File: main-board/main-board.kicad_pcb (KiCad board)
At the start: 2 copper layers, 56 parts, among them J1 MOTOR0, J10 PROGRAMMER, J11 CAM0, J12 CAM1, J13 CAM2, J14 CAM3, J15 CAM4, J16 CAM5, J17 CAM6, J18 CAM7, J19 PowerBoard Interface, J2 MOTOR1, J20 IMU Breakout, J3 MOTOR2, J4 MOTOR3, J5 RJ45, J6 MOTOR4, J7 MOTOR5, J8 MOTOR6, J9 MOTOR7, SW1 SW_SPST, T1 ATB2012E-50011M-T01, T2 ATB2012E-50011M-T01, U1 MCP2515-EST, U2 ATA6560, U3 ATmega2560-16AU | Main Proc, U4 MC14051B, U5 MC14051B, U6 SN75HVD3082EDR, U7 LTC1983ES6-5-TRPBF, U8 OPAMP, U9 OPAMP, Y1 20MHz, Y2 20MHz

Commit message: populate components
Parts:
- moved C6 147.5 mm to (89.9, 121.2), turned to 180 degrees
- moved R11 126.9 mm to (86.6, 85.3), turned to 270 degrees
- moved C2 122.9 mm to (93.8, 93.0), turned to 90 degrees
- moved C1 122.7 mm to (93.8, 89.6), turned to 270 degrees
- moved J17 81.2 mm to (142.9, 75.2), turned to 0 degrees
- moved J18 77.3 mm to (133.2, 75.4), turned to 0 degrees
- moved R9 73.7 mm to (89.9, 124.0)
- moved R10 70.4 mm to (76.8, 123.7)
- moved R8 70.2 mm to (89.9, 118.6)
- moved U4 65.0 mm to (136.9, 54.1)
- moved U5 64.8 mm to (125.7, 54.1)
- moved J16 64.7 mm to (142.9, 86.5), turned to 0 degrees
- moved J7 64.1 mm to (80.0, 45.3), turned to 180 degrees
- moved U6 63.7 mm to (83.4, 121.3), turned to 180 degrees
- moved J4 60.8 mm to (92.7, 45.3), turned to 180 degrees
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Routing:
- net CAN-: track 0.00 -> 199.4 mm, vias 0 -> 6
- net CAN+: track 0.00 -> 173.1 mm
- net +5V: track 0.00 -> 149.6 mm, vias 0 -> 2
- net GND: track 0.00 -> 124.5 mm
- net RS485+: track 0.00 -> 61.4 mm
- net SCL: track 0.00 -> 47.7 mm
- net SS: track 0.00 -> 36.9 mm, vias 0 -> 4
- net CAM1: track 0.00 -> 30.8 mm, vias 0 -> 2
- net CAM2: track 0.00 -> 28.8 mm, vias 0 -> 2
- net RS485-R: track 0.00 -> 26.6 mm
- net RS485-DIR: track 0.00 -> 25.7 mm, vias 0 -> 2
- net RESET-MAIN: track 0.00 -> 22.3 mm
- net -5V: track 0.00 -> 21.0 mm, vias 0 -> 2
- net CAM6: track 0.00 -> 16.7 mm, vias 0 -> 2
- net CAM5: track 0.00 -> 16.7 mm, vias 0 -> 2
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
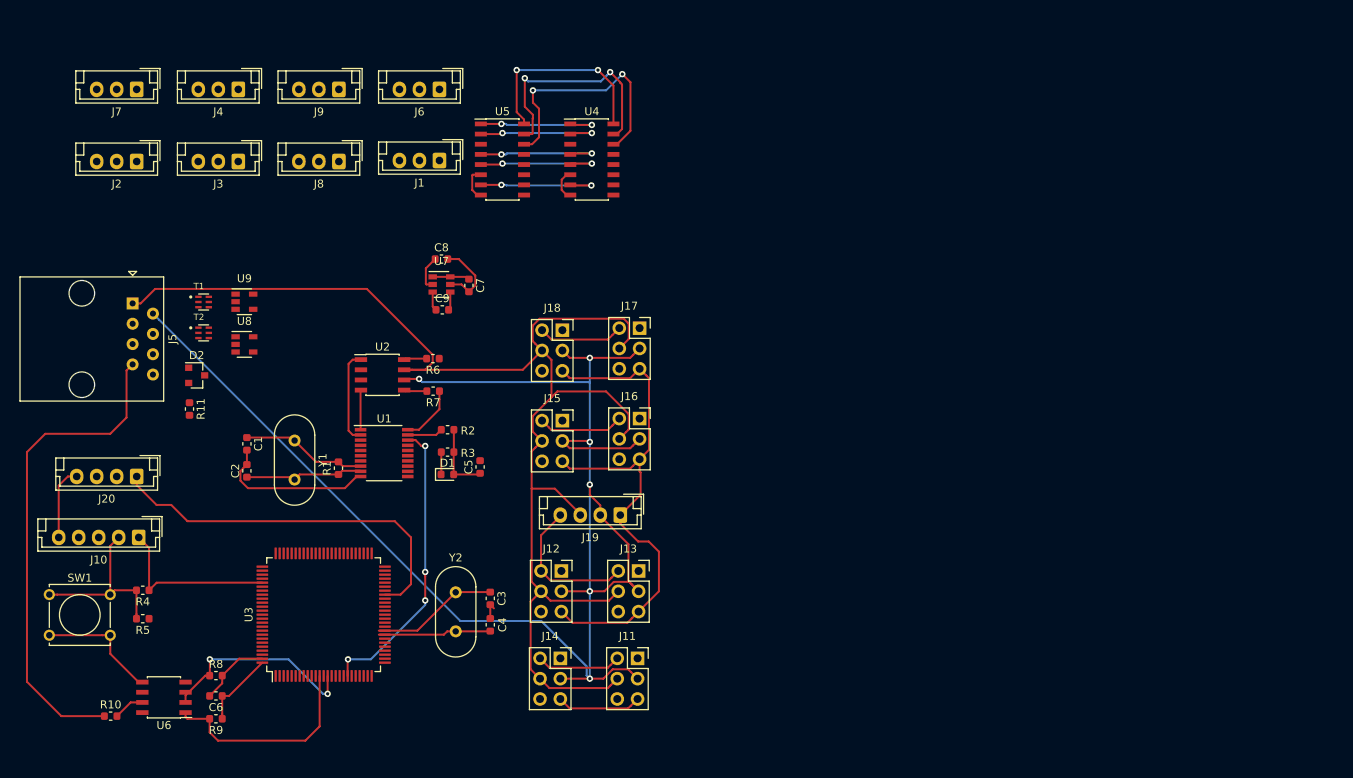
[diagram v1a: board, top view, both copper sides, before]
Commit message: add traces for all signals except cameras
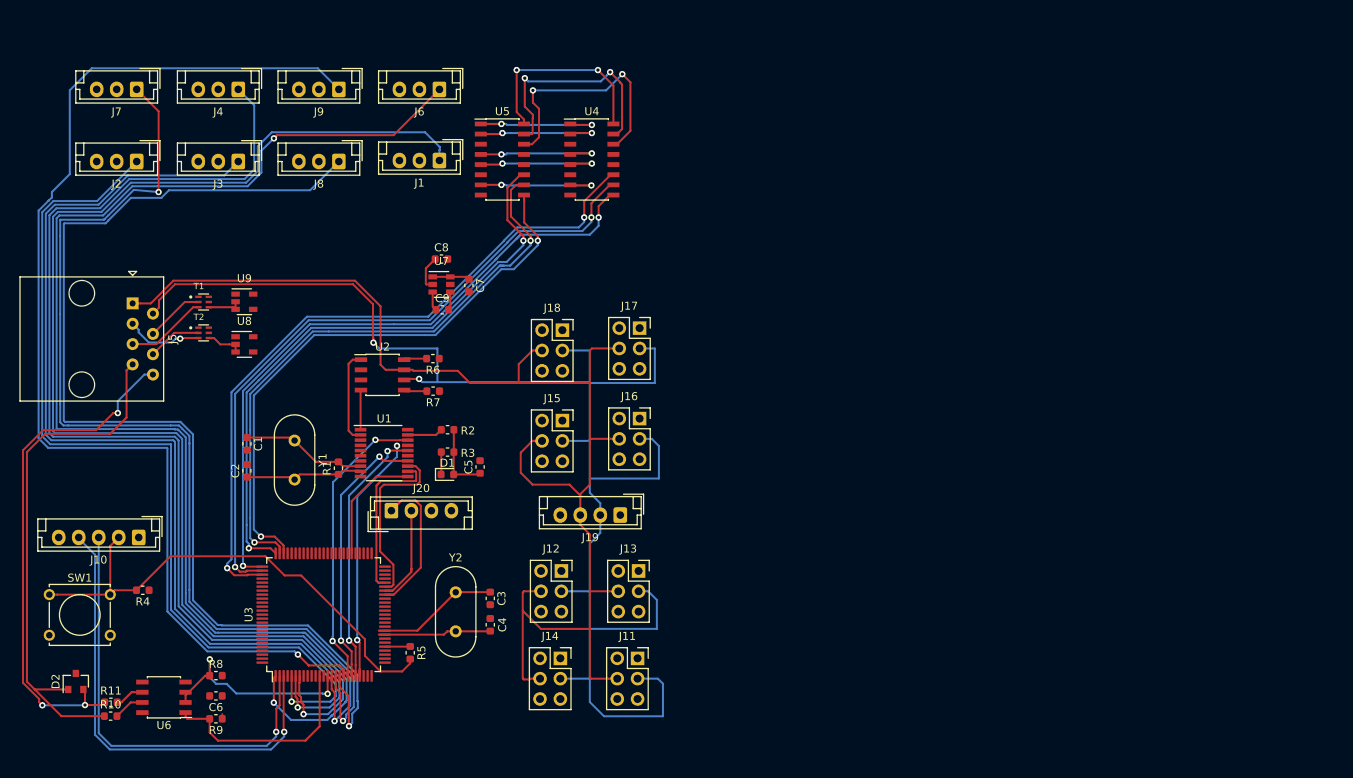
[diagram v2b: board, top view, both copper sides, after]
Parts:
- moved D2 41.1 mm to (72.4, 119.3), turned to 90 degrees
- moved R11 38.0 mm to (76.8, 122.0), turned to 0 degrees
- moved R5 33.7 mm to (114.2, 115.8), turned to 270 degrees
- moved J20 32.1 mm to (111.8, 98.0), turned to 0 degrees
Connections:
- U3 pad 73: VID12 -> VID1-2
- U3 pad 74: VID11 -> VID1-1
- U3 pad 75: VID10 -> VID1-0
- U3 pad 76: VID02 -> VID0-2
- U3 pad 77: VID01 -> VID0-1
- U3 pad 78: VID00 -> VID0-0
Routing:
- net M0: track 0.00 -> 162.6 mm, vias 0 -> 1
- net M4: track 0.00 -> 156.2 mm, vias 0 -> 2
- net M7: track 0.00 -> 143.9 mm, vias 0 -> 1
- net M3: track 0.00 -> 140.7 mm, vias 0 -> 1
- net M6: track 0.00 -> 137.9 mm, vias 0 -> 1
- net M2: track 0.00 -> 127.9 mm, vias 0 -> 1
- net M5: track 0.00 -> 127.6 mm, vias 0 -> 2
- net GND: track 124.5 -> 2.45 mm
- net +5V: track 149.6 -> 32.8 mm
- net M1: track 0.00 -> 114.6 mm, vias 0 -> 1
- net VID0-0: track 0.00 -> 87.6 mm, vias 0 -> 2
- net VID0-1: track 0.00 -> 84.9 mm, vias 0 -> 2
- net VID0-2: track 0.00 -> 83.4 mm, vias 0 -> 2
- net VID1-0: track 0.00 -> 76.8 mm, vias 0 -> 2
- net VID1-1: track 0.00 -> 76.2 mm, vias 0 -> 2
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
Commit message: complete electrical circuit, needs holes
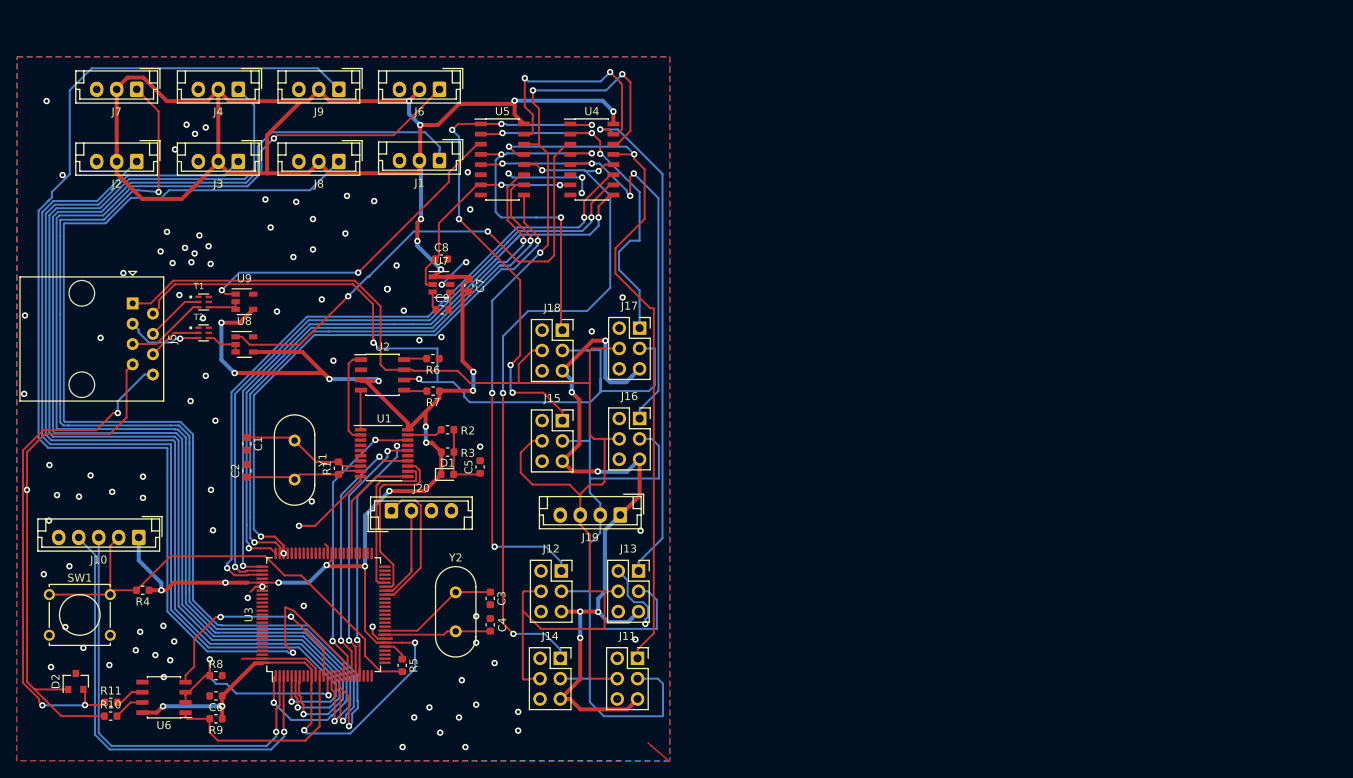
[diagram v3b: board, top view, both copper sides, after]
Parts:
- moved R5 1.87 mm to (113.2, 117.3)
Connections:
- U4 pad 3: VID0 -> VID-CAM0
- U5 pad 3: VID1 -> VID-CAM1
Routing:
- net +5V: track 32.8 -> 488.4 mm, vias 2 -> 31
- net CAM3: track 0.00 -> 89.1 mm, vias 0 -> 4
- net CAM0: track 0.00 -> 89.1 mm, vias 0 -> 2
- net CAM1: track 30.8 -> 95.3 mm, vias 2 -> 5
- net VID-CAM0: track 0.00 -> 63.0 mm, vias 0 -> 2
- net CAM2: track 28.8 -> 91.7 mm, vias 2 -> 3
- net GND: track 2.45 -> 55.9 mm, vias 0 -> 98
- net CAM4: track 16.7 -> 65.9 mm, vias 2 -> 6
- net VID-CAM1: track 0.00 -> 42.5 mm, vias 0 -> 2
- net CAM5: track 16.7 -> 59.2 mm, vias 2 -> 4
- net CAM7: track 16.7 -> 46.8 mm, vias 2 -> 3
- net CAM6: track 16.7 -> 46.4 mm, vias 2 -> 3
- net RS485-D: track 0.00 -> 29.0 mm, vias 0 -> 2
- net M7: track 143.9 -> 154.6 mm
- net -5V: track 21.0 -> 28.0 mm
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- added copper zone on B.Cu, net GND
- added copper zone on F.Cu, net GND
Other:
- net class +5V added: clearance 0.2, trace_width 0.5, via_dia 0.8, via_drill 0.4

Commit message: add mounting holes
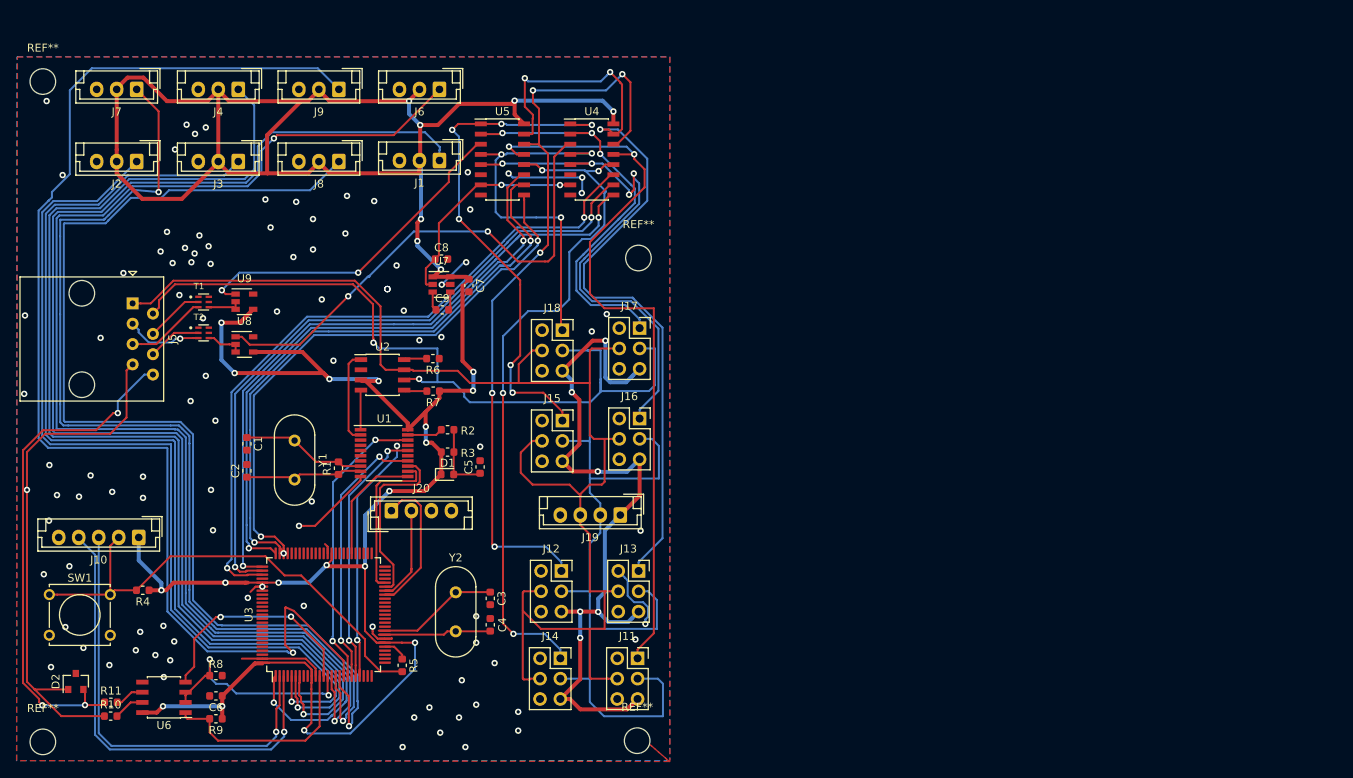
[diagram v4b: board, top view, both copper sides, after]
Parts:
- added REF**: MountingHole_3.2mm_M3, MountingHole:MountingHole_3.2mm_M3, F.Cu at (142.7, 66.4)
- added REF**: MountingHole_3.2mm_M3, MountingHole:MountingHole_3.2mm_M3, F.Cu at (142.6, 126.8)
- added REF**: MountingHole_3.2mm_M3, MountingHole:MountingHole_3.2mm_M3, F.Cu at (68.3, 44.4)
- added REF**: MountingHole_3.2mm_M3, MountingHole:MountingHole_3.2mm_M3, F.Cu at (68.3, 126.9)
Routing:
- net CAM2: track 91.7 -> 101.1 mm
- net CAM5: track 59.2 -> 68.0 mm
- net CAM0: track 89.1 -> 95.1 mm
- net CAM6: track 46.4 -> 52.4 mm
- net CAM3: track 89.1 -> 87.2 mm

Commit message: ready for review
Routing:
- net +5V: track 488.4 -> 501.1 mm, vias 31 -> 32
- net GND: track 55.9 -> 62.8 mm, vias 98 -> 99
- net CAM3: track 87.2 -> 84.2 mm
- net SO: track 31.8 -> 33.2 mm
- net CAM4: track 65.9 -> 66.8 mm

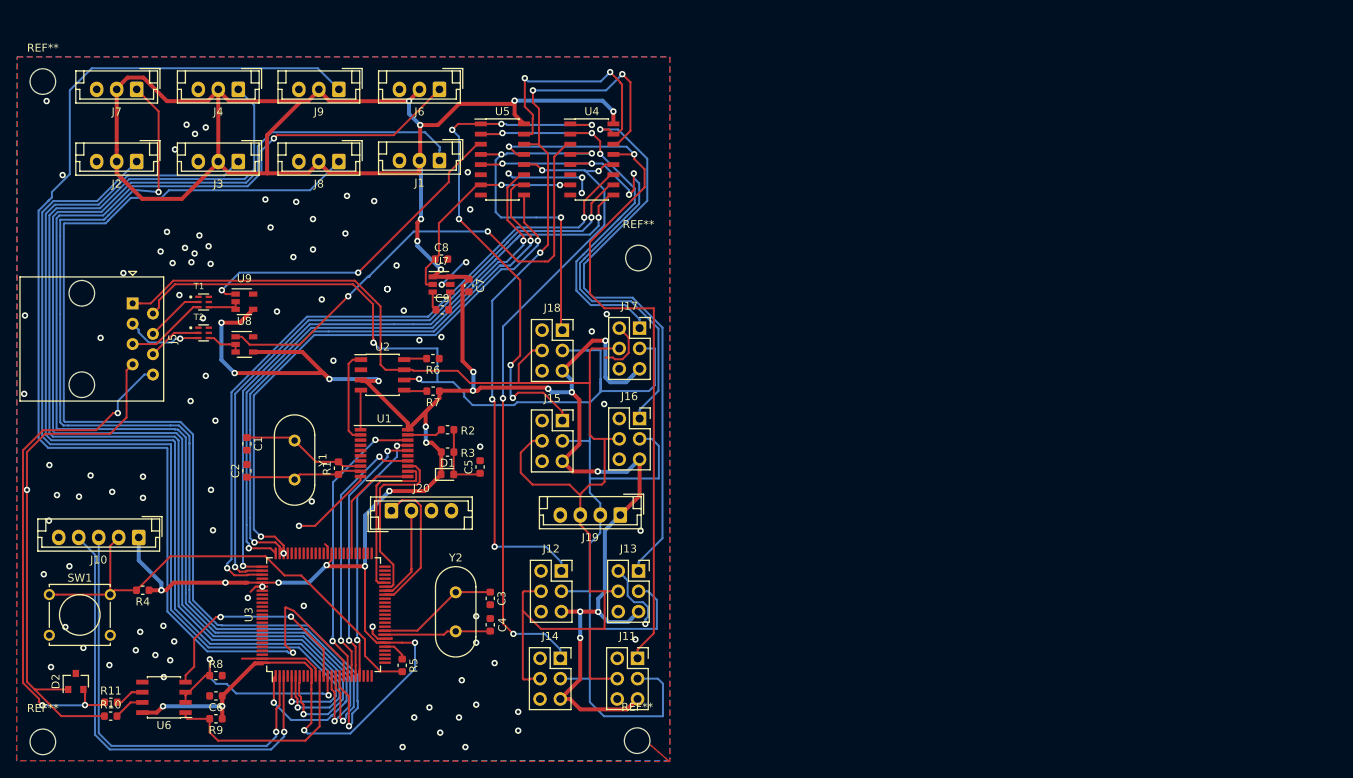
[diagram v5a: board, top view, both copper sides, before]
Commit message: Review+changes- see description
Schematic:
* add ICSP connector
* add VPP and diode D3for uC programming


PCB:
* add ICSP connector
* add VPP diode
* change tether connector from RJ45 to 2.54mm pitch 1x8 header
* slight silkscreen changes
* removed some overlapping vias
* moved vias from SMD pads
* slight changes to GND top copper pour



Requested before approval:
* silkscreen work
* Vinnie review


Requested other:
* Schematic formatting- boxes, labels, page layout, etc
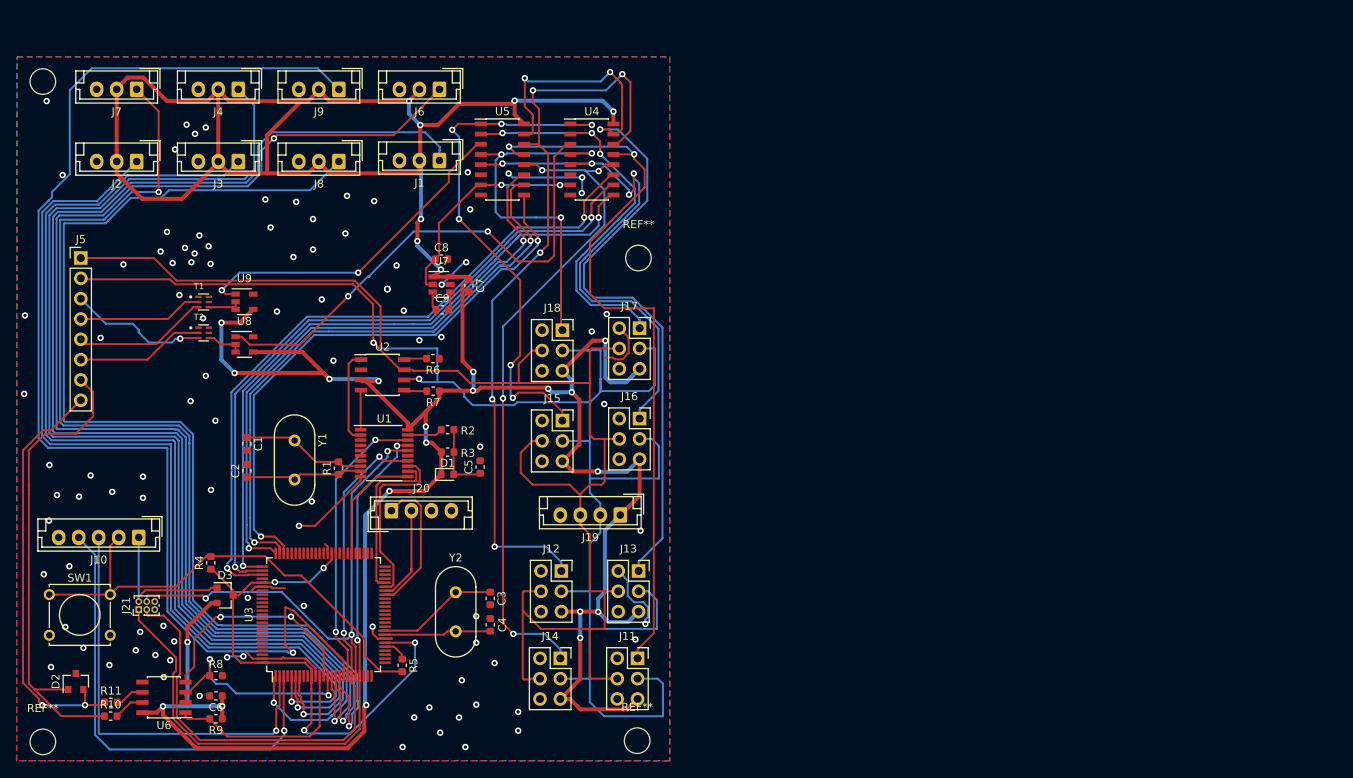
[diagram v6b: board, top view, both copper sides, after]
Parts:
- added D3: D_x2_KCom_AAK, Package_TO_SOT_SMD:SOT-23, F.Cu at (91.1, 108.6)
- added J21: ICSP (DO NOT POPULATE), Connector_PinHeader_1.00mm:PinHeader_2x03_P1.00mm_Vertical, F.Cu at (80.3, 110.4)
- J5: footprint Connector_RJ:RJ45_Amphenol_54602-x08_Horizontal -> Connector_PinHeader_2.54mm:PinHeader_1x08_P2.54mm_Vertical
- moved R4 9.17 mm to (89.3, 104.5), turned to 90 degrees
- moved J5 8.61 mm to (73.0, 66.4), turned to 0 degrees
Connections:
- J10 pad 1: +5V -> VPP
- R4 pad 1: +5V -> Net-(D3-Pad3)
- U3 pad 10: +5V -> Net-(D3-Pad3)
- U3 pad 100: +5V -> Net-(D3-Pad3)
- U3 pad 31: +5V -> Net-(D3-Pad3)
- U3 pad 61: +5V -> Net-(D3-Pad3)
- U3 pad 80: +5V -> Net-(D3-Pad3)
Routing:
- net Net-(D3-Pad3): track 0.00 -> 71.2 mm, vias 0 -> 4
- net SCK: track 33.7 -> 80.7 mm
- net SO: track 33.2 -> 80.0 mm
- net +5V: track 501.1 -> 469.8 mm, vias 32 -> 27
- net SI: track 33.0 -> 62.1 mm, vias 2 -> 3
- net VPP: track 0.00 -> 18.9 mm
- net RS485-: track 63.9 -> 52.7 mm, vias 3 -> 2
- net VID0-: track 6.79 -> 16.1 mm
- net VID1-: track 7.34 -> 15.6 mm
- net VID0+: track 9.61 -> 17.4 mm
- net CAN-: track 197.1 -> 204.4 mm
- net VID1+: track 10.1 -> 16.9 mm
- net RS485+: track 65.6 -> 59.5 mm, vias 1 -> 0
- net CAN+: track 172.8 -> 178.2 mm
- net GND: track 62.8 -> 67.7 mm, vias 99 -> 100
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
